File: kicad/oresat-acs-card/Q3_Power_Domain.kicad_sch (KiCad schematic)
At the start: 69 parts, among them Q31 MOSFET-PCH-SOT23-6, Q32 MOSFET-PCH-SOT23-6, Q33 PMV45EN2R, Q34 PMV45EN2R, Q35 MOSFET-PCH-dual-SOT23-6, U25 MAX7310ATE, U26 MAX4211FETE, U27 MIC842LYC5-TR, U28 MIC842LYC5-TR

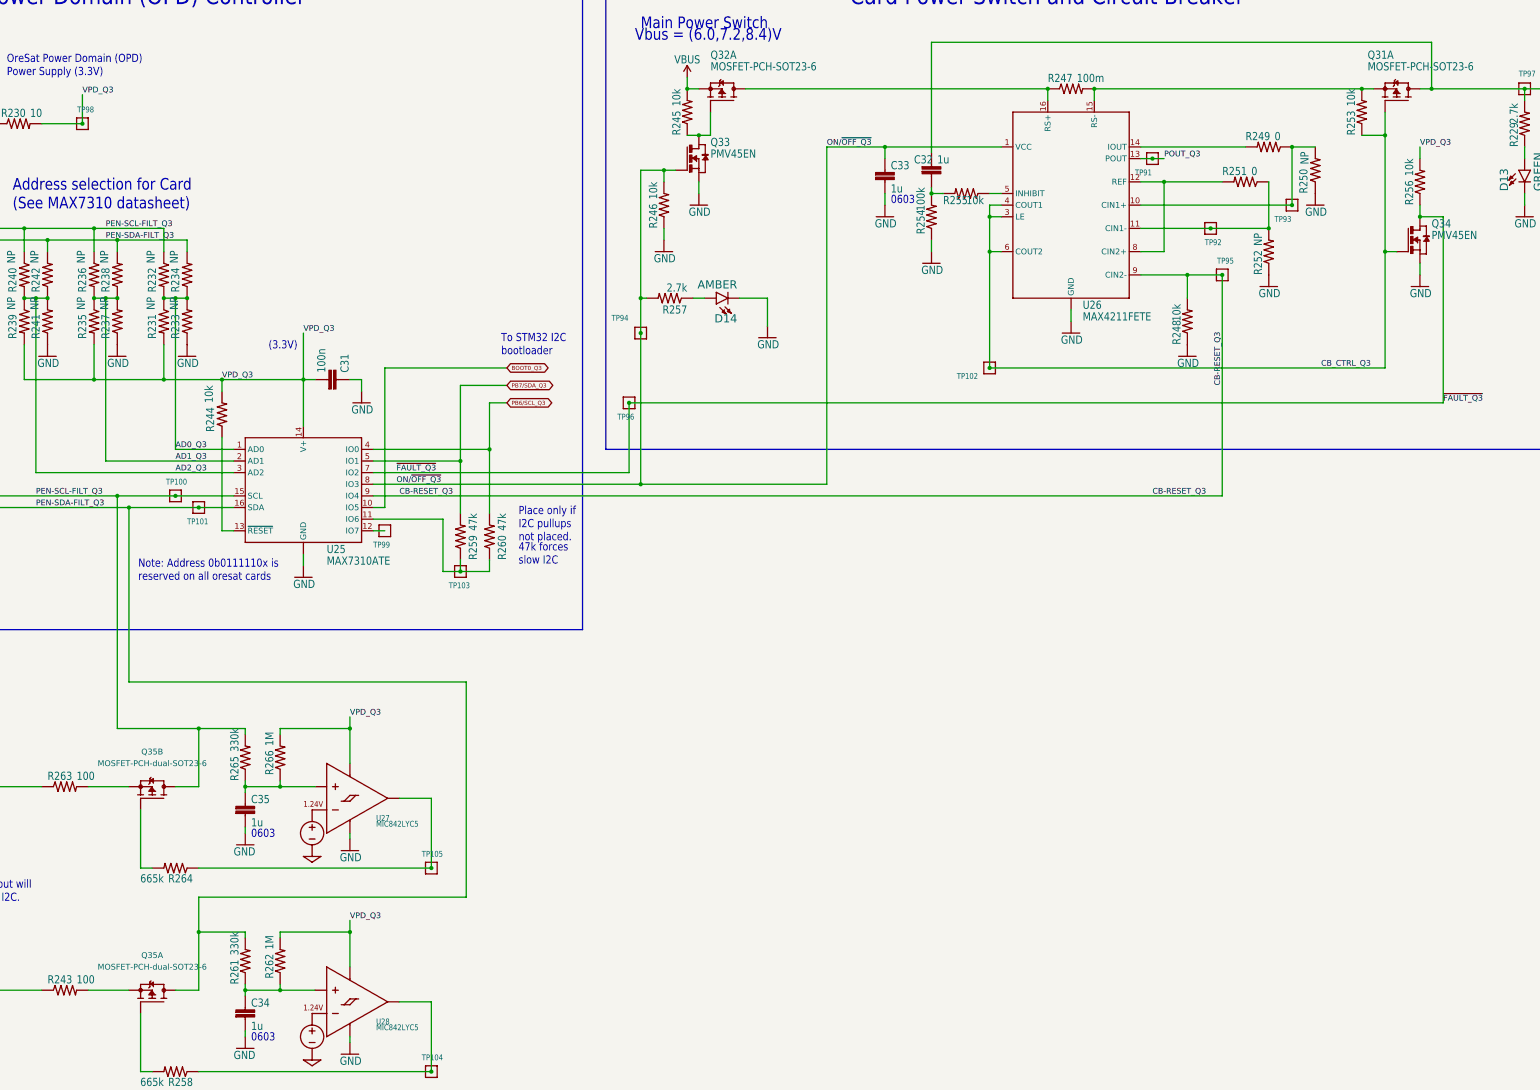
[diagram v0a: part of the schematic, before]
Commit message: Updated ACS board. Changed mezzanine pinouts. Added 5 V supplies for each quadrant. Updated layout.
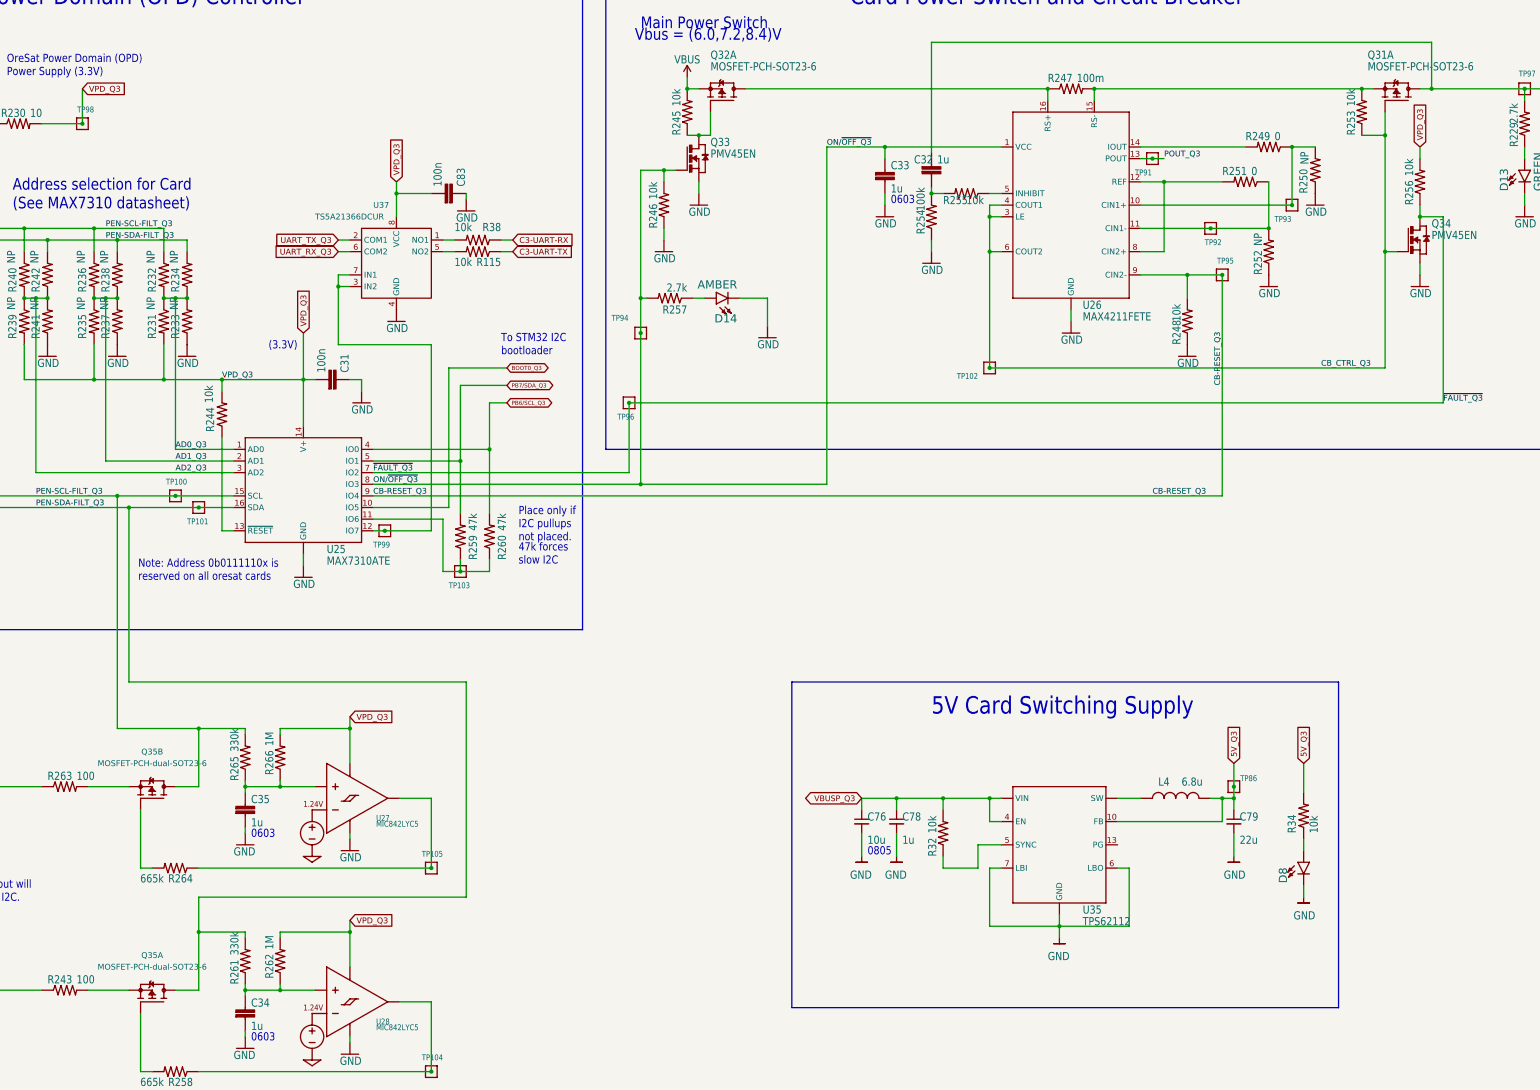
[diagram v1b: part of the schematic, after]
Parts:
- added C76: 10u, oresat-acs-card:.0805-B-NOSILK, symbol Device:C_Small
- added C78: 1u, Resistor_SMD:R_0603_1608Metric, symbol Device:C_Small
- added C79: 22u, Capacitor_SMD:C_1210_3225Metric, symbol Device:C_Small
- added C83: CL10B104KB8NNNL, oresat-acs-card:.0603-C-NOSILK, symbol oresat-acs-card-eagle-import:C-EU0603-C-NOSILK
- added D8: 150060VS55040, oresat-acs-card:LED-0603, symbol oresat-live-card-eagle-import:LED-GREEN0603
- added L4: 6.8u, oresat-acs-card:ECS-MPI4040, symbol oresat-live-card-eagle-import:L-ECS-MPI4040
- added R115, R38: RC0603FR-0710KL, oresat-acs-card:.0603-C-NOSILK, symbol oresat-acs-card-eagle-import:R-US_0603-C-NOSILK
- added R32, R34: 10k, Resistor_SMD:R_0603_1608Metric, symbol oresat-live-card-eagle-import:R-US_0603-A
- added TP86: TEST-POINT-LARGE-SQUARE, oresat-acs-card:1X01, symbol oresat-acs-card-eagle-import:TEST-POINT-LARGE-SQUARE
- added U35: TPS62112, oresat-acs-card:S-PVQFN-16, symbol oresat-live-card-eagle-import:TPS6211X
- added U37: TS5A21366DCUR, oresat-acs-card:DCU-R-PDSO-G8, symbol oresat-acs-card-eagle-import:TS5A21366DCUR
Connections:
- net GND: now also C76.2, C78.2, C79.2, C83.1, D8.C, U35.1 (GND), U35.11 (GND), U35.12 (GND), U35.16 (GND), U35.6 (LBO), U35.7 (LBI), U35.9 (GND), U35.PAD (GND), U37.4 (GND)
- net VBUSP_Q3: now also C76.1, C78.1, R32.2, U35.2 (VIN), U35.3 (VIN), U35.4 (EN), U35.8 (VIN)
- net VPD_Q3: now also C83.2, U37.8 (VCC)
- net at TP99.1, U25.12 (IO7): now also U37.3 (IN2), U37.7 (IN1)
- new net: R115.2, U37.5 (NO2)
- new net: R38.2, U37.1 (NO1)
- new net: D8.A, R34.1
- new net: L4.1, U35.14 (SW), U35.15 (SW)
- new net: R32.1, U35.5 (SYNC)
- new net 5V_Q3: C79.1, L4.2, R34.2, TP86.1, U35.10 (FB)
- new net C3-UART-RX: R38.1
- new net C3-UART-TX: R115.1
- new net UART_RX_Q3: U37.6 (COM2)
- new net UART_TX_Q3: U37.2 (COM1)
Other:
- note added: "0805"
- note added: "5V Card Switching Supply"

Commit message: Updated 5 V regulator and tweaked card layout. Cleaned up silkscreen layer and schematic.
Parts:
- removed L4: 6.8u, oresat-acs-card:ECS-MPI4040, symbol oresat-live-card-eagle-import:L-ECS-MPI4040
- removed R32, R34: 10k, Resistor_SMD:R_0603_1608Metric, symbol oresat-live-card-eagle-import:R-US_0603-A
- removed U35: TPS62112, oresat-acs-card:S-PVQFN-16, symbol oresat-live-card-eagle-import:TPS6211X
- added L4: 3u3, Inductor_SMD:L_Coilcraft_XxL4030, symbol Device:L_Small
- added R32, R33, R34: 100k, Resistor_SMD:R_0603_1608Metric, symbol Device:R_Small_US
- added U35: LTC3624, Package_DFN_QFN:DFN-8-1EP_3x3mm_P0.5mm_EP1.65x2.38mm, symbol U-Linear Tech-LTC3624:LTC3624
- C76: footprint oresat-acs-card:.0805-B-NOSILK -> Capacitor_SMD:C_0805_2012Metric; Distributor DigiKey -> (none); MPN CGA4J1X7R0J106M125AC -> (none)
- C78: value 1u -> 2u2; footprint Resistor_SMD:R_0603_1608Metric -> Capacitor_SMD:C_0603_1608Metric; Distributor DigiKey -> (none); MPN CGA3E1X7R1E105M080AE -> (none)
- C79: value 22u -> 47u; footprint Capacitor_SMD:C_1210_3225Metric -> Capacitor_SMD:C_1206_3216Metric; Distributor DigiKey -> (none); MFR (none) -> KYOCERA AVX; MPN CGA6P1X7R1C226M250AC -> 1206YD476MAT2A
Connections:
- net 5V_Q3: now also L4.2, R34.1, U35.5 (FB)
- net GND: now also R33.2, U35.8 (GND), U35.9 (GND)
- net VBUSP_Q3: now also U35.2 (Vin), U35.3 (RUN); no longer C78.1
- net at D8.A: now also R34.2
- new net: L4.1, U35.1 (SW)
- new net: C78.1, R32.1, U35.6 (INTVcc)
- new net: R32.2, R33.1, U35.7 (MODE)
- no-connect marks 0 -> 1
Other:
- note removed: "0805"
- moved on the sheet: C31, C32, C33, C34, C35, C83, D13, D14, D8, Q31A, Q32A, Q33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

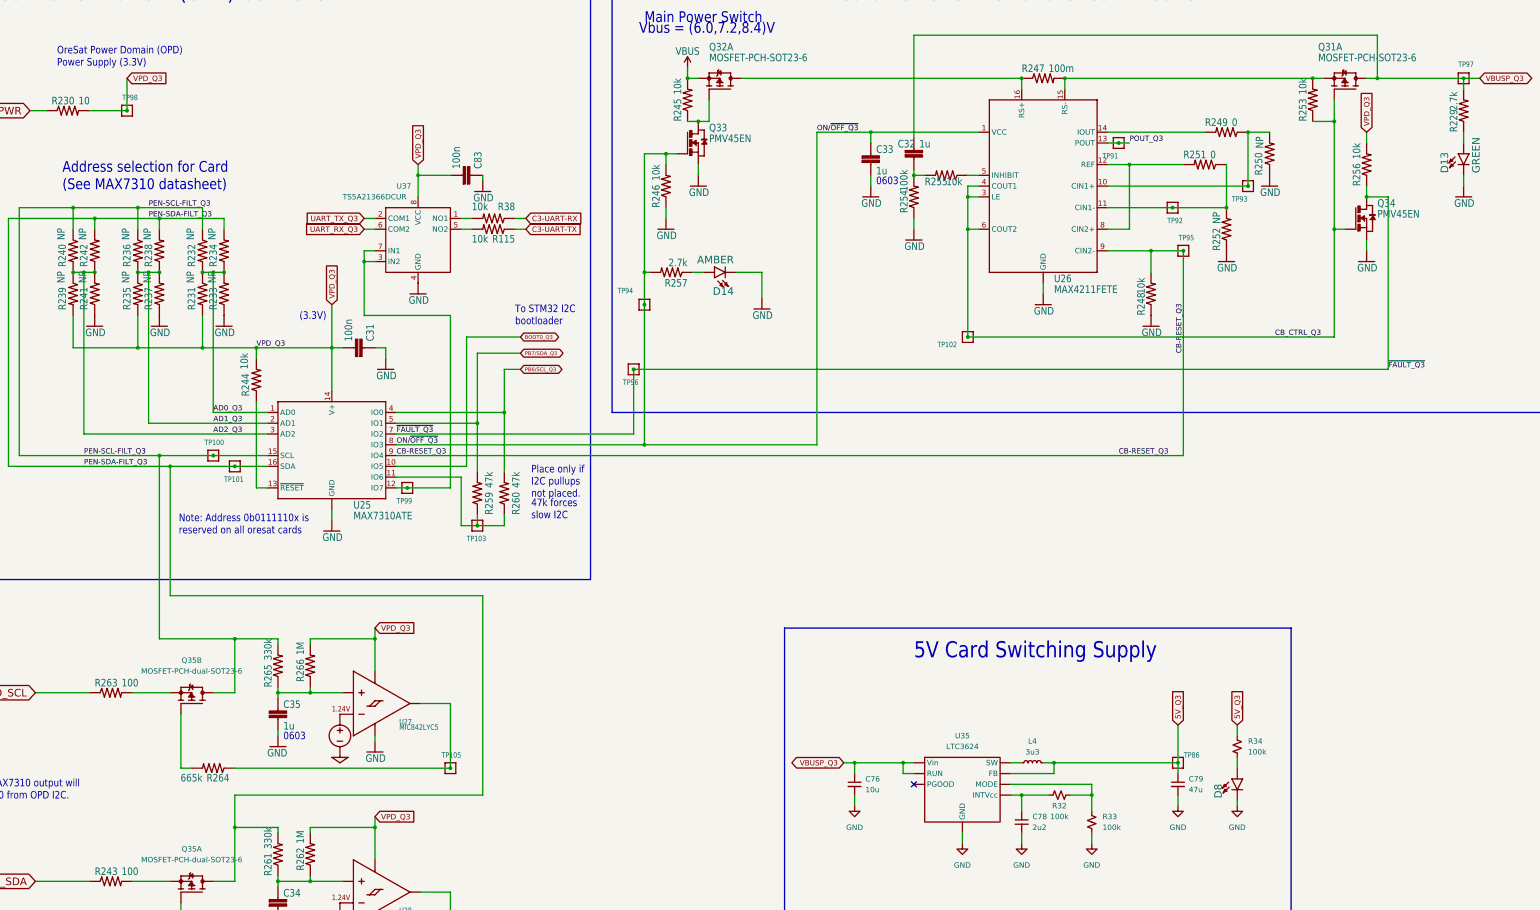
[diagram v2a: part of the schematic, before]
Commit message: Updated 5V regulators to match design block. Added UART switch to microcontroller. Added power flags and cleaned up ERC errors
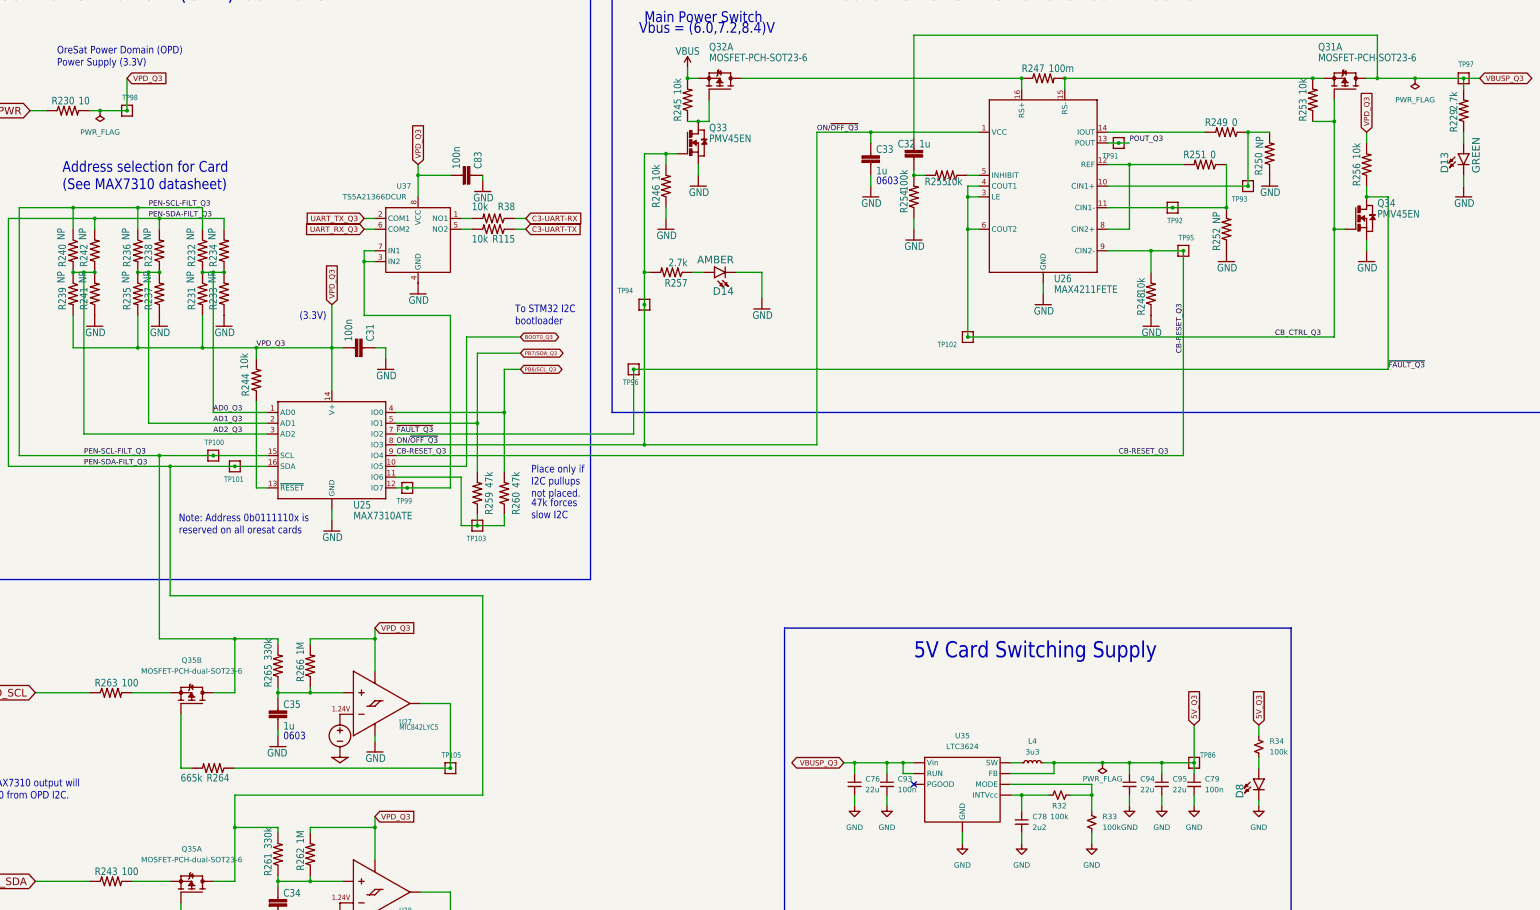
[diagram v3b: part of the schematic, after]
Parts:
- added C93: 100n, Capacitor_SMD:C_0603_1608Metric, symbol Device:C_Small
- added C94, C95: 22u, Capacitor_SMD:C_1210_3225Metric, symbol Device:C_Small
- C76: value 10u -> 22u; footprint Capacitor_SMD:C_0805_2012Metric -> Capacitor_SMD:C_1210_3225Metric
- C79: value 47u -> 100n; footprint Capacitor_SMD:C_1206_3216Metric -> Capacitor_SMD:C_0603_1608Metric
- D8: value 150060VS55040 -> LED-GREEN0603; symbol oresat-live-card-eagle-import:LED-GREEN0603 -> oresat-acs-card-eagle-import:LED-GREEN0603
- L4: footprint Inductor_SMD:L_Coilcraft_XxL4030 -> oresat-footprints:L_ECS-MPI4040
- U35: footprint Package_DFN_QFN:DFN-8-1EP_3x3mm_P0.5mm_EP1.65x2.38mm -> oresat-footprints:DFN-8-1EP_3x3mm_P0.5mm_EP1.65x2.38mm_ThermalVias0.3mm
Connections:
- net 5V_Q3: now also C94.1, C95.1
- net GND: now also C93.2, C94.2, C95.2
- net VBUSP_Q3: now also C93.1
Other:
- moved on the sheet: C79, D8, R34, TP86

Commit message: Design review changes.
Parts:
- R34: value 100k -> 10k
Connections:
- net VPD_Q3: no longer C83.2, U37.8 (VCC)
- net ON/~{OFF_Q3} renamed ON/~{OFF}_Q3
- net ON/~{OFF}_Q3: now also C83.2, U37.8 (VCC)
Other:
- note added: "Resistor values TBD"
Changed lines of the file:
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@@
   (junction (at 64.77 69.85) (diameter 0) (color 0 0 0 0)
   )
+  (junction (at 194.31 54.61) (diameter 0) (color 0 0 0 0)
+  )
   (junction (at 154.94 118.11) (diameter 0) (color 0 0 0 0)
   )
@@
     (stroke (width 0) (type default) (color 0 0 0 0))
   )
+  (wire (pts (xy 194.31 54.61) (xy 140.97 54.61))
+    (stroke (width 0) (type default) (color 0 0 0 0))
+  )
   (wire (pts (xy 154.94 142.24) (xy 161.29 142.24))
     (stroke (width 0) (type default) (color 0 0 0 0))
@@
     (stroke (width 0) (type default) (color 0 0 0 0))
   )
-  (wire (pts (xy 140.97 57.15) (xy 140.97 59.69))
+  (wire (pts (xy 140.97 54.61) (xy 140.97 59.69))
     (stroke (width 0) (type default) (color 0 0 0 0))
   )
@@
     (effects (font (size 3.81 3.2385)) (justify left bottom))
   )
+  (text "Resistor values TBD" (at 304.8 45.72 0)
+    (effects (font (size 1.27 1.27)) (justify left bottom))
+  )
   (text "> 100 ms low on MAX7310 output will\ndisconnect MAX7310 from OPD I2C."
     (at 21.59 207.01 0)
@@
     (effects (font (size 3.81 3.2385)) (justify left bottom))
   )
+  (label "ON/~{OFF}_Q3" (at 194.31 69.215 90)
+    (effects (font (size 1.2446 1.2446)) (justify left bottom))
+  )
   (label "~{FAULT_Q3}" (at 369.57 105.41 0)
     (effects (font (size 1.2446 1.2446)) (justify left bottom))
@@
     (effects (font (size 1.2446 1.2446)) (justify left bottom))
   )
-  (label "ON/~{OFF_Q3}" (at 135.89 123.19 0)
+  (label "ON/~{OFF}_Q3" (at 140.97 54.61 0)
+    (effects (font (size 1.2446 1.2446)) (justify left bottom))
+  )
+  (label "ON/~{OFF}_Q3" (at 135.89 123.19 0)
     (effects (font (size 1.2446 1.2446)) (justify left bottom))
   )
@@
     (effects (font (size 1.2446 1.2446)) (justify left bottom))
   )
-  (label "ON/~{OFF_Q3}" (at 234.95 49.53 0)
+  (label "ON/~{OFF}_Q3" (at 234.95 49.53 0)
     (effects (font (size 1.2446 1.2446)) (justify left bottom))
   )
@@
     )
   )
-  (global_label "VPD_Q3" (shape input) (at 140.97 57.15 90) (fields_autoplaced)
-    (effects (font (size 1.27 1.27)) (justify left))
-    (property "Intersheet References" "${INTERSHEET_REFS}" (id 0) (at 140.8906 47.6007 90)
-      (effects (font (size 1.27 1.27)) (justify left) hide)
-    )
-  )
   (global_label "VBUSP_Q3" (shape bidirectional) (at 391.16 36.83 0) (fields_autoplaced)
     (effects (font (size 1.2446 1.2446)) (justify left))
@@
       (effects (font (size 1.27 1.27)) (justify left))
     )
-    (property "Value" "100k" (id 1) (at 341.63 195.5799 0)
+    (property "Value" "10k" (id 1) (at 341.63 195.5799 0)
       (effects (font (size 1.27 1.27)) (justify left))
     )
@@
       (effects (font (size 1.778 1.5113)) (justify left bottom))
     )
-    (property "Value" "2.7k" (id 1) (at 386.08 44.45 0)
+    (property "Value" "10k" (id 1) (at 386.08 44.45 0)
       (effects (font (size 1.778 1.5113)) (justify left bottom))
     )
@@
   (symbol (lib_id "oresat-acs-card-eagle-import:C-EU0603-C-NOSILK") (at 153.67 59.69 270) (mirror x) (unit 1)
     (in_bom yes) (on_board yes)
-    (property "Reference" "C83" (id 0) (at 154.051 58.166 0)
+    (property "Reference" "C83" (id 0) (at 154.305 56.515 90)
       (effects (font (size 1.778 1.5113)) (justify left bottom))
     )
-    (property "Value" "100n" (id 1) (at 148.971 58.166 0)
+    (property "Value" "100n" (id 1) (at 144.78 56.515 90)
       (effects (font (size 1.778 1.5113)) (justify left bottom))
     )
@@
       (effects (font (size 1.778 1.5113)) (justify left bottom))
     )
-    (property "Value" "2.7k" (id 1) (at 204.47 79.248 0)
+    (property "Value" "4.7k" (id 1) (at 204.47 79.248 0)
       (effects (font (size 1.778 1.5113)) (justify left bottom))
     )
